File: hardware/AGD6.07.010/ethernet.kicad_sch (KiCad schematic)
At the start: 11 parts, among them J1001 PX_ETH GH4, J1002 SIYI_ETH GH4, J1003 CAMF_ETH GH4, J1004 AI_ETH1 GH4, J1005 SERVICE_ETH GH4, J1006 AI_ETH2 GH4, J1007 ETH_SWITCH_MODULE 2x13, J1008 CAMD_ETH GH4

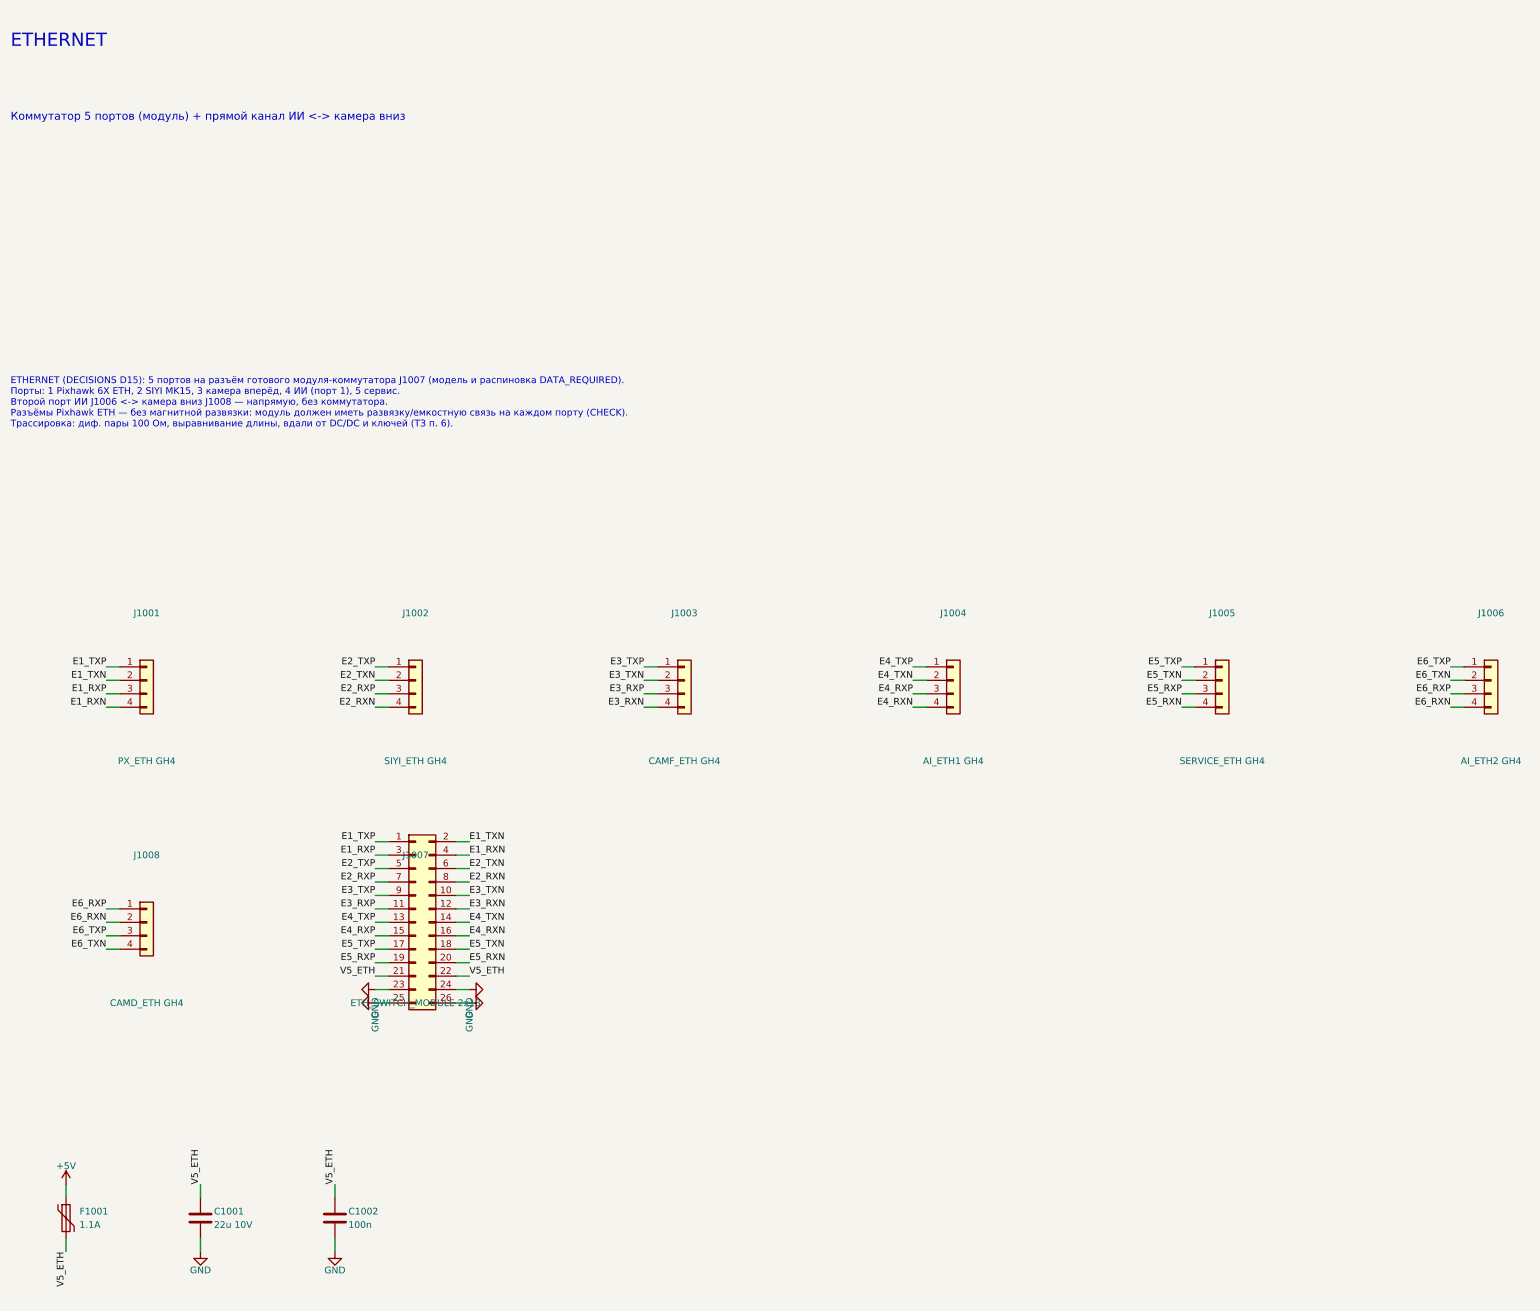
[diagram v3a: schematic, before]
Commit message: AGD6.07.010 rev 0.4 (WIP): 3x TRACO THL40 DC/DC, split 12 V bus, SwitchBlox Ethernet, fixed LM5069 UVLO/OVLO, computed hot-swap values, PX4 firmware notes; board re-placed, routing in progress
Co-Authored-By: Claude Opus 5.5 <noreply@anthropic.com>
Claude-Session: https://claude.ai/code/session_01Qk7uTKdi6YbndB9fGuguYV
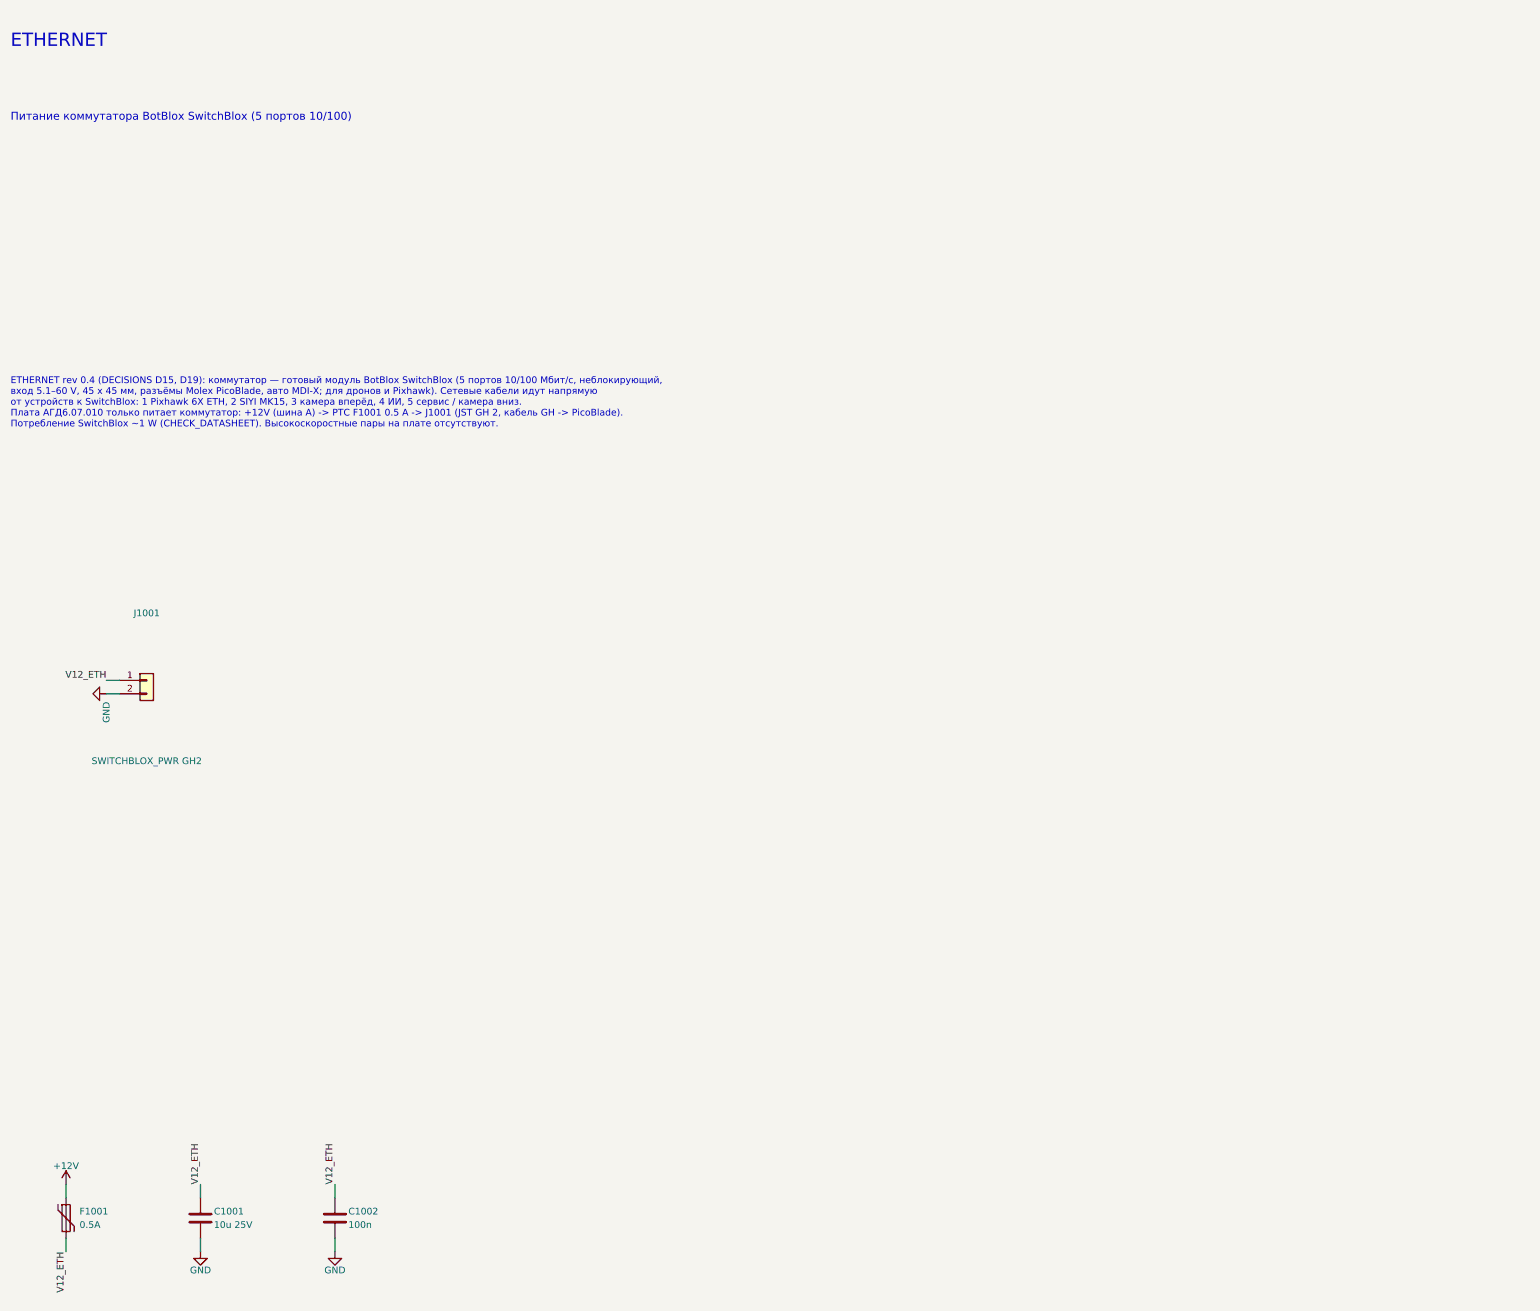
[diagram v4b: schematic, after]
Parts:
- removed J1001: PX_ETH GH4, Connector_JST:JST_GH_SM04B-GHS-TB_1x04-1MP_P1.25mm_Horizontal, symbol Connector_Generic:Conn_01x04
- removed J1002: SIYI_ETH GH4, Connector_JST:JST_GH_SM04B-GHS-TB_1x04-1MP_P1.25mm_Horizontal, symbol Connector_Generic:Conn_01x04
- removed J1003: CAMF_ETH GH4, Connector_JST:JST_GH_SM04B-GHS-TB_1x04-1MP_P1.25mm_Horizontal, symbol Connector_Generic:Conn_01x04
- removed J1004: AI_ETH1 GH4, Connector_JST:JST_GH_SM04B-GHS-TB_1x04-1MP_P1.25mm_Horizontal, symbol Connector_Generic:Conn_01x04
- removed J1005: SERVICE_ETH GH4, Connector_JST:JST_GH_SM04B-GHS-TB_1x04-1MP_P1.25mm_Horizontal, symbol Connector_Generic:Conn_01x04
- removed J1006: AI_ETH2 GH4, Connector_JST:JST_GH_SM04B-GHS-TB_1x04-1MP_P1.25mm_Horizontal, symbol Connector_Generic:Conn_01x04
- removed J1007: ETH_SWITCH_MODULE 2x13, Connector_PinHeader_2.54mm:PinHeader_2x13_P2.54mm_Vertical, symbol Connector_Generic:Conn_02x13_Odd_Even
- removed J1008: CAMD_ETH GH4, Connector_JST:JST_GH_SM04B-GHS-TB_1x04-1MP_P1.25mm_Horizontal, symbol Connector_Generic:Conn_01x04
- added J1001: SWITCHBLOX_PWR GH2, Connector_JST:JST_GH_SM02B-GHS-TB_1x02-1MP_P1.25mm_Horizontal, symbol Connector_Generic:Conn_01x02
- C1001: value 22u 10V -> 10u 25V; footprint Capacitor_SMD:C_0805_2012Metric -> Capacitor_SMD:C_1210_3225Metric
- F1001: value 1.1A -> 0.5A; footprint Fuse:Fuse_1812_4532Metric -> Fuse:Fuse_1206_3216Metric
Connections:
- net GND: now also J1001.2 (Pin_2)
- net +5V renamed +12V
- net V5_ETH renamed V12_ETH
- net V12_ETH: now also J1001.1 (Pin_1)
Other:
- note added: "ETHERNET rev 0.4 (DECISIONS D15, D19): коммутатор — готовый модуль BotBlox SwitchBlox (5 портов 10/100 Мбит/с, неблокирующий, вход 5.1–60 V, 45 x 45 мм, разъёмы Molex PicoBlade, авто MDI-X; для дронов и Pixhawk). Сетевые кабели идут напрямую от устройств к SwitchBlox: 1 Pixhawk 6X ETH, 2 SIYI MK15, 3 камера вперёд, 4 ИИ, 5 сервис / камера вниз. Плата АГД6.07.010 только питает коммутатор: +12V (ши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"
- note added: "Питание коммутатора BotBlox SwitchBlox (5 портов 10/100)"
- note removed: "ETHERNET (DECISIONS D15): 5 портов на разъём готового модуля-коммутатора J1007 (модель и распиновка DATA_REQUIRED). Порты: 1 Pixhawk 6X ETH, 2 SIYI MK15, 3 камера вперёд, 4 ИИ (порт 1), 5 сервис. Второй порт ИИ J1006 <-> камера вниз J1008 — напрямую, без коммутатора. Разъёмы Pixhawk ETH — без магнитной развязки: модуль должен иметь развязку/емкостную связь на каждом порту (CHECK). Трассировка: ди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"
- note removed: "Коммутатор 5 портов (модуль) + прямой канал ИИ <-> камера вниз"
